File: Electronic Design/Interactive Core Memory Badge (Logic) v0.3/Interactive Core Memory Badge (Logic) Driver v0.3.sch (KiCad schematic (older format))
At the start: 67 parts, among them J1 Conn_01x16_Male, J2 Conn_01x16_Male, Q1 MMBT4401LT1G, Q10 MMBT4401LT1G, Q11 MMBT4403LT1G, Q12 MMBT4401LT1G, Q13 MMBT4403LT1G, Q14 MMBT4401LT1G, Q15 MMBT4403LT1G, Q16 MMBT4401LT1G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

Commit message: Add I2C bus, clean-up power symbols, update MCU sheet.
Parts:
- J1, J2: value Conn_01x16_Male -> Conn_01x16_Female; symbol Connector:Conn_01x16_Male -> Connector:Conn_01x16_Female
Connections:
- net labels added: I2C_CLOCK, I2C_DATA
- wire segments 219 -> 217
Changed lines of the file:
@@
 Wire Wire Line
 	2450 2000 2550 2000
-Text GLabel 1250 1800 2    50   Output ~ 0
+Text GLabel 1450 1800 2    50   Output ~ 0
 YL1
-Text GLabel 1250 1700 2    50   Output ~ 0
+Text GLabel 1450 1700 2    50   Output ~ 0
 YL0
-Text GLabel 1250 1900 2    50   Output ~ 0
+Text GLabel 1450 1900 2    50   Output ~ 0
 YL2
-Text GLabel 1250 2000 2    50   Output ~ 0
+Text GLabel 1450 2000 2    50   Output ~ 0
 YL3
-Text GLabel 1250 2100 2    50   Output ~ 0
-YL4
-Text GLabel 1250 2200 2    50   Output ~ 0
-YL5
-Text GLabel 1250 2300 2    50   Output ~ 0
-YL6
-Text GLabel 1250 2400 2    50   Output ~ 0
+Text GLabel 1450 2400 2    50   Output ~ 0
 YL7
 Wire Wire Line
-	1200 2100 1200 2300
-Wire Wire Line
-	1200 2300 1250 2300
-Wire Wire Line
-	1250 1700 800  1700
-Wire Wire Line
-	1250 2000 800  2000
-Wire Wire Line
-	1250 2100 1200 2100
-Wire Wire Line
-	1200 2100 800  2100
-Connection ~ 1200 2100
-Wire Wire Line
-	1150 2400 1250 2400
-Wire Wire Line
-	1150 2200 1150 2400
-Wire Wire Line
-	1250 2200 1150 2200
+	1400 2100 1400 2300
+Wire Wire Line
+	1400 2300 1450 2300
+Wire Wire Line
+	1450 1700 800  1700
+Wire Wire Line
+	1450 2000 800  2000
+Wire Wire Line
+	1450 2100 1400 2100
+Wire Wire Line
+	1400 2100 800  2100
+Connection ~ 1400 2100
+Wire Wire Line
+	1350 2400 1450 2400
+Wire Wire Line
+	1350 2200 1350 2400
+Wire Wire Line
+	1450 2200 1350 2200
 Text Notes 600  1400 0    50   ~ 0
 YL: 6\nSENSE: 2\nSPARE: 2\nGND, 3V3: 2\nMHS: 4 (hall switches)\nTOTAL=16
 Wire Wire Line
-	1150 2200 800  2200
-Connection ~ 1150 2200
+	1350 2200 800  2200
+Connection ~ 1350 2200
 Wire Wire Line
 	2450 2800 2550 2800
@@
 	2450 2700 2550 2700
 $Comp
-L Connector:Conn_01x16_Male J2
+L Connector:Conn_01x16_Female J2
 U 1 1 5E78B5ED
 P 2750 2400
-F 0 "J2" H 3300 3350 50  0000 C CNN
-F 1 "Conn_01x16_Male" H 3050 3250 50  0000 C CNN
+F 0 "J2" H 2100 3350 50  0000 C CNN
+F 1 "Conn_01x16_Female" H 2400 3250 50  0000 C CNN
 F 2 "Connector_PinSocket_2.54mm:PinSocket_1x16_P2.54mm_Vertical_SMD_Pin1Left" H 2750 2400 50  0001 C CNN
 F 3 "~" H 2750 2400 50  0001 C CNN
 	1    2750 2400
-	-1   0    0    -1
-$EndComp
-$Comp
-L Connector:Conn_01x16_Male J1
+	1    0    0    -1
+$EndComp
+$Comp
+L Connector:Conn_01x16_Female J1
 U 1 1 5E78B5F3
 P 600 2400
-F 0 "J1" H 700 3350 50  0000 C CNN
-F 1 "Conn_01x16_Male" H 950 3250 50  0000 C CNN
+F 0 "J1" H 550 3350 50  0000 C CNN
+F 1 "Conn_01x16_Female" H 250 3250 50  0000 C CNN
 F 2 "Connector_PinSocket_2.54mm:PinSocket_1x16_P2.54mm_Vertical_SMD_Pin1Left" H 600 2400 50  0001 C CNN
 F 3 "~" H 600 2400 50  0001 C CNN
 	1    600  2400
-	1    0    0    -1
+	-1   0    0    -1
 $EndComp
 Text Notes 1950 1400 0    50   ~ 0
@@
 Wire Wire Line
 	2450 2600 2550 2600
-Text GLabel 1250 2500 2    50   Input ~ 0
+Text GLabel 900  2300 2    50   Input ~ 0
 SENSE1
-Text GLabel 1250 2600 2    50   Input ~ 0
+Text GLabel 900  2400 2    50   Input ~ 0
 SENSE2
 Wire Wire Line
-	1100 2500 1250 2500
-Wire Wire Line
-	1100 2300 1100 2500
-Wire Wire Line
-	1250 2600 1050 2600
-Wire Wire Line
-	1050 2600 1050 2400
-Wire Wire Line
-	1050 2400 800  2400
+	900  2400 800  2400
 Text GLabel 2500 3000 0    50   Input ~ 0
 LED_MATRIX
@@
 	1600 2800 1600 3050
 Wire Wire Line
-	800  2700 1100 2700
+	800  2700 900  2700
 Wire Wire Line
 	800  2800 1600 2800
@@
 	1    0    0    -1
 $EndComp
-Text GLabel 1100 2700 2    50   Input ~ 0
+Text GLabel 900  2700 2    50   Input ~ 0
 3V3_100mA
 Wire Wire Line
-	800  1800 1250 1800
-Wire Wire Line
-	800  1900 1250 1900
-Wire Wire Line
-	800  2300 1100 2300
+	800  1800 1450 1800
+Wire Wire Line
+	800  1900 1450 1900
+Wire Wire Line
+	800  2300 900  2300
 Wire Wire Line
 	800  2900 850  2900
@@
 	2100 2900 2550 2900
 Text Notes 2350 3200 0    50   ~ 0
-N/C
-Text Notes 850  2550 0    50   ~ 0
-N/C
-Text Notes 850  2650 0    50   ~ 0
 N/C
 Wire Wire Line
@@
 Wire Wire Line
 	1250 7400 1250 7500
+Text GLabel 900  2500 2    50   BiDi ~ 0
+I2C_CLOCK
+Text GLabel 900  2600 2    50   BiDi ~ 0
+I2C_DATA
+Text GLabel 1450 2300 2    50   Output ~ 0
+YL6
+Text GLabel 1450 2200 2    50   Output ~ 0
+YL5
+Text GLabel 1450 2100 2    50   Output ~ 0
+YL4
+Wire Wire Line
+	800  2500 900  2500
+Wire Wire Line
+	800  2600 900  2600
 $EndSCHEMATC

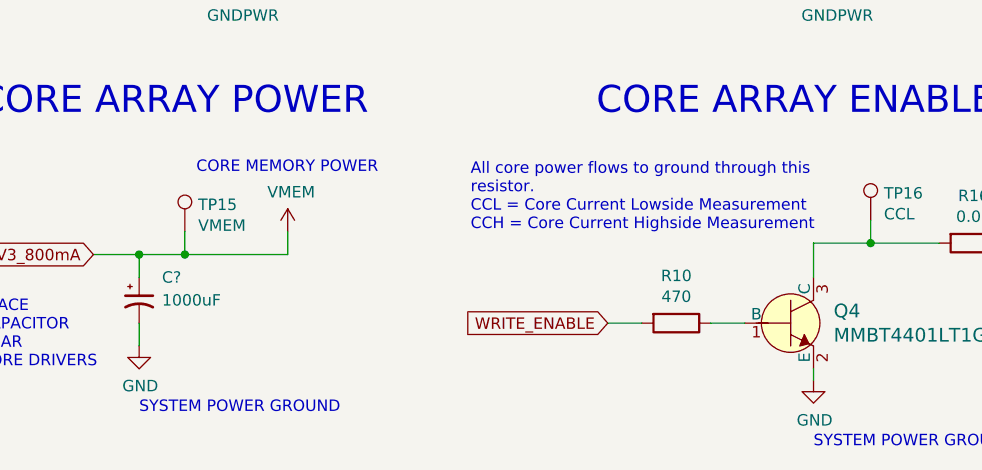
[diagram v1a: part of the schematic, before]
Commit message: Add sense NORs and IO expansion and NOTs.
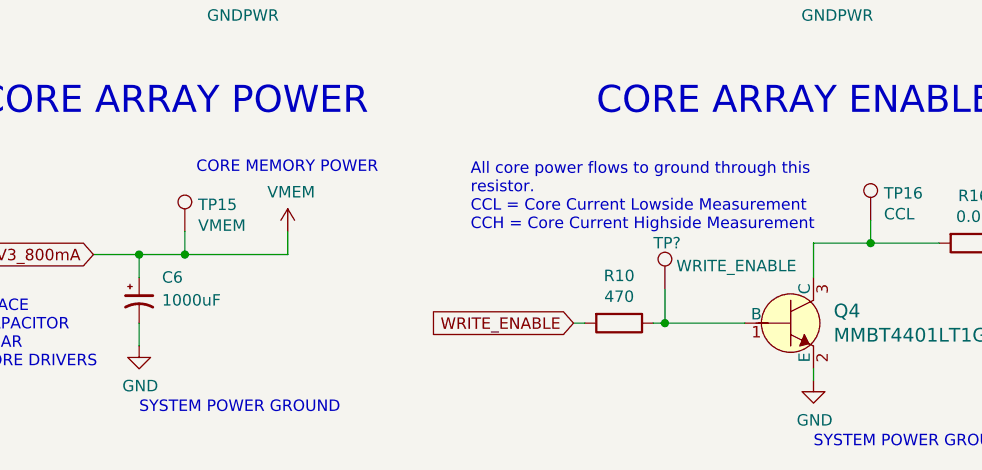
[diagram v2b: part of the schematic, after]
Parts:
- added TP?: WRITE_ENABLE, TestPoint:TestPoint_Keystone_5000-5004_Miniature, symbol Connector:TestPoint
- gave numbers to parts that had none: 1
- renumbered Q1 to Q4, R1 to R10, R2 to R16, TP1 to TP15, TP2 to TP16, TP3 to TP17
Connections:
- net at Q4.1 (B), R10.1: now also TP?.1
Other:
- moved on the sheet: R10
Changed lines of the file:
@@
 $Descr A 11000 8500
 encoding utf-8
-Sheet 4 5
+Sheet 4 6
 Title "Core 64 - Core Array Driver"
 Date "2020-03-15"
@@
 Text Notes 8700 5550 0    50   ~ 0
 ROW 2,6
-Text GLabel 3300 7400 0    50   Input ~ 0
+Text GLabel 3150 7400 0    50   Input ~ 0
 WRITE_ENABLE
 Text Notes 5250 7450 0    50   ~ 0
 CORE MEMORY GROUND
 $Comp
-L Digikey-Transistors:MMBT4401LT1G Q1
+L Digikey-Transistors:MMBT4401LT1G Q?
 U 1 1 5E8ED55F
 P 4100 7400
-AR Path="/5E8ED55F" Ref="Q1"  Part="1"
+AR Path="/5E8ED55F" Ref="Q?"  Part="1"
 AR Path="/5D254AE8/5E8ED55F" Ref="Q?"  Part="1"
 AR Path="/5E755AC8/5E8ED55F" Ref="Q4"  Part="1"
@@
 	4200 7050 4200 7200
 $Comp
-L Device:R R1
+L Device:R R?
 U 1 1 5E8ED566
-P 3600 7400
-AR Path="/5E8ED566" Ref="R1"  Part="1"
+P 3350 7400
+AR Path="/5E8ED566" Ref="R?"  Part="1"
 AR Path="/5D254AE8/5E8ED566" Ref="R?"  Part="1"
 AR Path="/5E755AC8/5E8ED566" Ref="R10"  Part="1"
-F 0 "R10" V 3393 7400 50  0000 C CNN
-F 1 "470" V 3484 7400 50  0000 C CNN
-F 2 "Resistor_SMD:R_0805_2012Metric" V 3530 7400 50  0001 C CNN
-F 3 "~" H 3600 7400 50  0001 C CNN
-	1    3600 7400
+F 0 "R10" V 3143 7400 50  0000 C CNN
+F 1 "470" V 3234 7400 50  0000 C CNN
+F 2 "Resistor_SMD:R_0805_2012Metric" V 3280 7400 50  0001 C CNN
+F 3 "~" H 3350 7400 50  0001 C CNN
+	1    3350 7400
 	0    1    1    0
 $EndComp
 Wire Wire Line
-	3750 7400 3900 7400
-$Comp
-L power:GNDPWR #PWR0101
+	3500 7400 3550 7400
+$Comp
+L power:GNDPWR #PWR?
 U 1 1 5E8ED56D
 P 5300 7150
-AR Path="/5E8ED56D" Ref="#PWR0101"  Part="1"
+AR Path="/5E8ED56D" Ref="#PWR?"  Part="1"
 AR Path="/5D254AE8/5E8ED56D" Ref="#PWR?"  Part="1"
 AR Path="/5E755AC8/5E8ED56D" Ref="#PWR0151"  Part="1"
@@
 $EndComp
 Wire Wire Line
-	3300 7400 3450 7400
+	3150 7400 3200 7400
 Text Notes 1500 6750 0    50   ~ 0
 CORE MEMORY POWER
 $Comp
-L Device:R R2
+L Device:R R?
 U 1 1 5E8ED580
 P 4900 7050
-AR Path="/5E8ED580" Ref="R2"  Part="1"
+AR Path="/5E8ED580" Ref="R?"  Part="1"
 AR Path="/5D254AE8/5E8ED580" Ref="R?"  Part="1"
 AR Path="/5E755AC8/5E8ED580" Ref="R16"  Part="1"
@@
 P 4450 6950
 AR Path="/5D254AE8/5E8ED587" Ref="TP?"  Part="1"
-AR Path="/5E8ED587" Ref="TP2"  Part="1"
+AR Path="/5E8ED587" Ref="TP?"  Part="1"
 AR Path="/5E755AC8/5E8ED587" Ref="TP16"  Part="1"
 F 0 "TP16" H 4508 7068 50  0000 L CNN
@@
 P 5300 6950
 AR Path="/5D254AE8/5E8ED58D" Ref="TP?"  Part="1"
-AR Path="/5E8ED58D" Ref="TP3"  Part="1"
+AR Path="/5E8ED58D" Ref="TP?"  Part="1"
 AR Path="/5E755AC8/5E8ED58D" Ref="TP17"  Part="1"
 F 0 "TP17" H 5358 7068 50  0000 L CNN
@@
 P 4200 7650
 AR Path="/5D254AE8/5E8ED59A" Ref="#PWR?"  Part="1"
-AR Path="/5E8ED59A" Ref="#PWR0102"  Part="1"
+AR Path="/5E8ED59A" Ref="#PWR?"  Part="1"
 AR Path="/5E755AC8/5E8ED59A" Ref="#PWR0152"  Part="1"
 F 0 "#PWR0152" H 4200 7400 50  0001 C CNN
@@
 P 2100 3100
 AR Path="/5D254AE8/5E79F49F" Ref="#PWR?"  Part="1"
-AR Path="/5E79F49F" Ref="#PWR0104"  Part="1"
+AR Path="/5E79F49F" Ref="#PWR?"  Part="1"
 AR Path="/5E755AC8/5E79F49F" Ref="#PWR0165"  Part="1"
 F 0 "#PWR0165" H 2100 2850 50  0001 C CNN
@@
 CORE BOARD INTERCONNECTS
 $Comp
-L power:+VSW #PWR?
+L power:+VSW #PWR0122
 U 1 1 5E76A192
 P 2100 2850
-F 0 "#PWR?" H 2100 2700 50  0001 C CNN
+F 0 "#PWR0122" H 2100 2700 50  0001 C CNN
 F 1 "+VSW" H 2115 3025 50  0000 C CNN
 F 2 "" H 2100 2850 50  0001 C CNN
@@
 P 1450 7000
 AR Path="/5D254AE8/5E8ED577" Ref="TP?"  Part="1"
-AR Path="/5E8ED577" Ref="TP1"  Part="1"
+AR Path="/5E8ED577" Ref="TP?"  Part="1"
 AR Path="/5E755AC8/5E8ED577" Ref="TP15"  Part="1"
 F 0 "TP15" H 1508 7118 50  0000 L CNN
@@
 AR Path="/5E755787/5E91F406" Ref="C?"  Part="1"
 AR Path="/5E755AC8/5D2551FF/5E91F406" Ref="C?"  Part="1"
-AR Path="/5E755AC8/5E91F406" Ref="C?"  Part="1"
-F 0 "C?" H 1350 7400 50  0000 L CNN
+AR Path="/5E755AC8/5E91F406" Ref="C6"  Part="1"
+F 0 "C6" H 1350 7400 50  0000 L CNN
 F 1 "1000uF" H 1350 7300 50  0000 L CNN
 F 2 "Capacitor_SMD:CP_Elec_8x10" H 1250 7300 50  0001 C CNN
@@
 AR Path="/5D254AE8/5E94D2F4" Ref="#PWR?"  Part="1"
 AR Path="/5E94D2F4" Ref="#PWR?"  Part="1"
-AR Path="/5E755AC8/5E94D2F4" Ref="#PWR?"  Part="1"
-F 0 "#PWR?" H 1250 7250 50  0001 C CNN
+AR Path="/5E755AC8/5E94D2F4" Ref="#PWR0126"  Part="1"
+F 0 "#PWR0126" H 1250 7250 50  0001 C CNN
 F 1 "GND" H 1255 7325 50  0000 C CNN
 F 2 "" H 1250 7500 50  0001 C CNN
@@
 Wire Wire Line
 	800  2600 900  2600
+$Comp
+L Connector:TestPoint TP?
+U 1 1 5E9A49E8
+P 3550 7250
+AR Path="/5E755787/5E9A49E8" Ref="TP?"  Part="1"
+AR Path="/5E755AC8/5D2551FF/5E9A49E8" Ref="TP?"  Part="1"
+AR Path="/5E755AC8/5E9A49E8" Ref="TP?"  Part="1"
+F 0 "TP?" H 3500 7450 50  0000 L CNN
+F 1 "WRITE_ENABLE" H 3600 7350 50  0000 L CNN
+F 2 "TestPoint:TestPoint_Keystone_5000-5004_Miniature" H 3750 7250 50  0001 C CNN
+F 3 "~" H 3750 7250 50  0001 C CNN
+	1    3550 7250
+	1    0    0    -1
+$EndComp
+Wire Wire Line
+	3550 7250 3550 7400
+Connection ~ 3550 7400
+Wire Wire Line
+	3550 7400 3900 7400
 $EndSCHEMATC

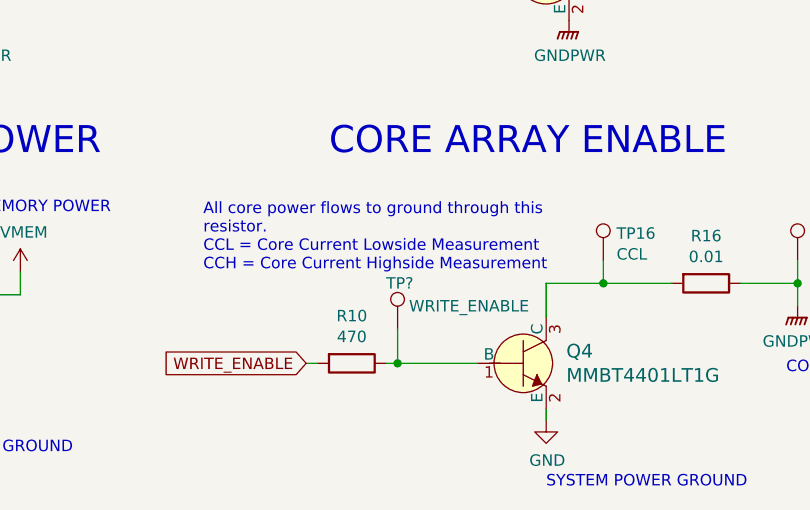
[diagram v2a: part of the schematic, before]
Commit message: Create PDF schematics
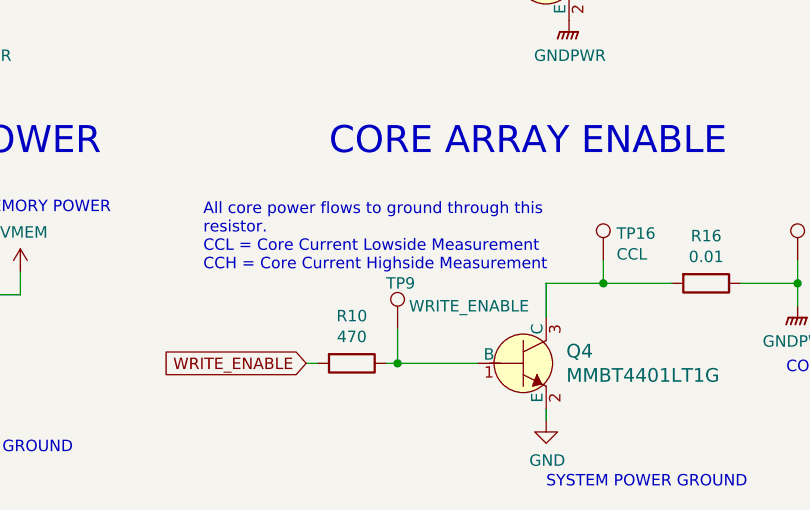
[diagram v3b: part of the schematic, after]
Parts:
- gave numbers to parts that had none: 1
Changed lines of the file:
@@
 AR Path="/5E755787/5E9A49E8" Ref="TP?"  Part="1"
 AR Path="/5E755AC8/5D2551FF/5E9A49E8" Ref="TP?"  Part="1"
-AR Path="/5E755AC8/5E9A49E8" Ref="TP?"  Part="1"
-F 0 "TP?" H 3500 7450 50  0000 L CNN
+AR Path="/5E755AC8/5E9A49E8" Ref="TP9"  Part="1"
+F 0 "TP9" H 3500 7450 50  0000 L CNN
 F 1 "WRITE_ENABLE" H 3600 7350 50  0000 L CNN
 F 2 "TestPoint:TestPoint_Keystone_5000-5004_Miniature" H 3750 7250 50  0001 C CNN

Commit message: Schematic refinement
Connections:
- net LED_MATRIX renamed LED_MATRIX_+VSW
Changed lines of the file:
@@
 $Descr A 11000 8500
 encoding utf-8
-Sheet 4 6
+Sheet 2 5
 Title "Core 64 - Core Array Driver"
 Date "2020-03-15"
@@
 	900  2400 800  2400
 Text GLabel 2500 3000 0    50   Input ~ 0
-LED_MATRIX
+LED_MATRIX_+VSW
 Wire Wire Line
 	2500 3000 2550 3000

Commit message: Update SMD-TO pad sizes, add EEPROM, add RasPI header to LED array
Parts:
- J1, J2: footprint Connector_PinSocket_2.54mm:PinSocket_1x16_P2.54mm_Vertical_SMD_Pin1Left -> Connector_PinHeader_2.54mm:PinHeader_1x16_P2.54mm_Vertical_SMD_and_TH_Pin1Left
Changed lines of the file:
@@
 F 0 "J2" H 2100 3350 50  0000 C CNN
 F 1 "Conn_01x16_Female" H 2400 3250 50  0000 C CNN
-F 2 "Connector_PinSocket_2.54mm:PinSocket_1x16_P2.54mm_Vertical_SMD_Pin1Left" H 2750 2400 50  0001 C CNN
+F 2 "Connector_PinHeader_2.54mm:PinHeader_1x16_P2.54mm_Vertical_SMD_and_TH_Pin1Left" H 2750 2400 50  0001 C CNN
 F 3 "~" H 2750 2400 50  0001 C CNN
 	1    2750 2400
@@
 F 0 "J1" H 550 3350 50  0000 C CNN
 F 1 "Conn_01x16_Female" H 250 3250 50  0000 C CNN
-F 2 "Connector_PinSocket_2.54mm:PinSocket_1x16_P2.54mm_Vertical_SMD_Pin1Left" H 600 2400 50  0001 C CNN
+F 2 "Connector_PinHeader_2.54mm:PinHeader_1x16_P2.54mm_Vertical_SMD_and_TH_Pin1Left" H 600 2400 50  0001 C CNN
 F 3 "~" H 600 2400 50  0001 C CNN
 	1    600  2400
